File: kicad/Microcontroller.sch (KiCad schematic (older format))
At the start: 25 parts, among them J10 CONN_01X06, J7 Vin, J8 Foot Switch, J9 CONN_01X06, Q3 IRF740, U3 LM2575, U4 MAX6675

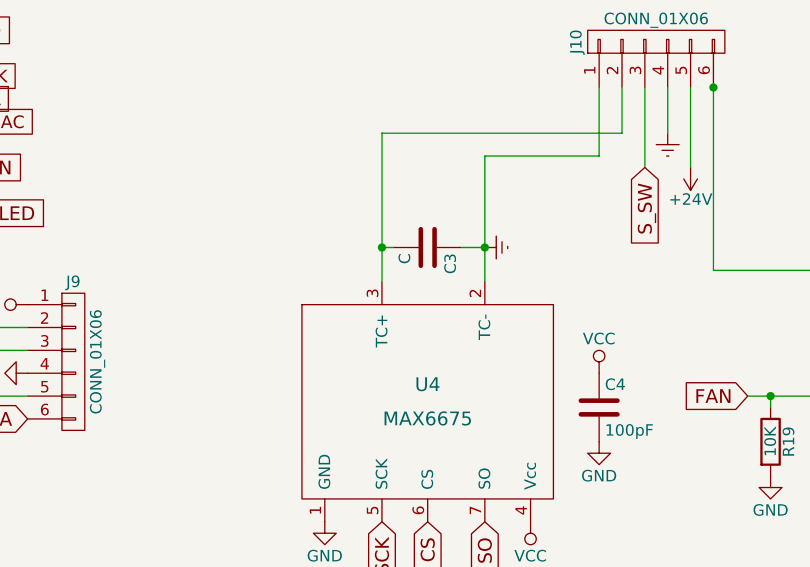
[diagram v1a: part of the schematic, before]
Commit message: Added C6 bypass capacitor
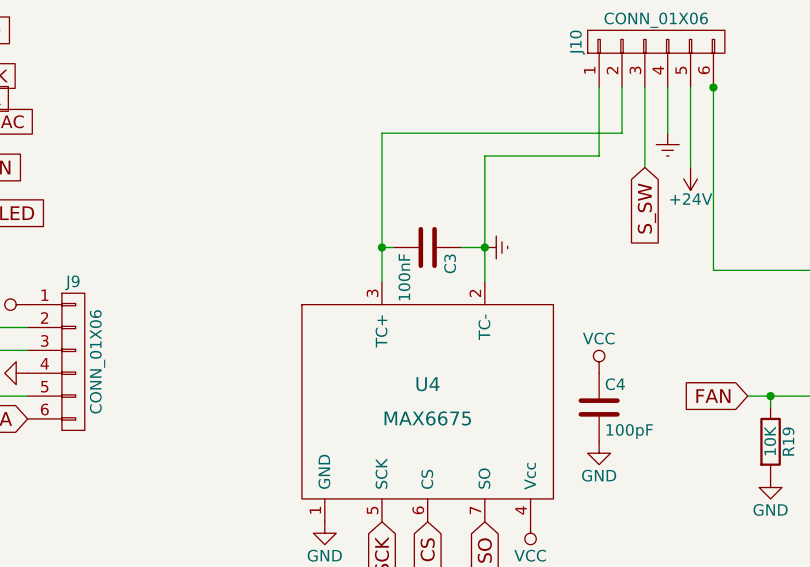
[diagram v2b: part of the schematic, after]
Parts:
- C3: value C -> 100nF
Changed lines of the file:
@@
 P 7200 3050
 F 0 "C3" H 7225 3150 50  0000 L CNN
-F 1 "C" H 7225 2950 50  0000 L CNN
+F 1 "100nF" H 7225 2950 50  0000 L CNN
 F 2 "Capacitors_SMD:C_0603_HandSoldering" H 7238 2900 50  0001 C CNN
 F 3 "" H 7200 3050 50  0001 C CNN
